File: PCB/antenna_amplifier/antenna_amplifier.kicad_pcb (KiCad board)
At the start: 4 copper layers, 200 x 100 mm, 131 parts, among them J101 PWR_IN 9V, J201 FILT_IN, J202 BIAS, J401 AES3 OUT, J402 S/PDIF OUT, SW301 RESET, SW302 PCM1804 MODE, SW401 CS8406 MODE, U101 ADM7150ARDZ-5.0, U102 ADM7150ARDZ-3.3, U201 LMP7721, U202 LMP7715, U203 LMP7715, U301 LMP7715, U302 PCM1804, U401 CS8406, Y401 24.576MHz

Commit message: Add mechanical design, PSU placement table and status notes (checkpoint)
mechanical/: CadQuery sources, STEP, DXF and renders for the amplifier
shield (7 mm flat-bar frame, milled tray, lid), PSU box, air-gap plate
capacitor assembly and the outdoor enclosure fit check (Fibox ARCA
403015). STATUS.md lists what is done and the next steps.

Co-Authored-By: Claude Opus 5.5 <noreply@anthropic.com>
Claude-Session: https://claude.ai/code/session_01RsM1DhHhY1tSr2aHjVygSC
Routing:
- added copper zone on In1.Cu, net GND

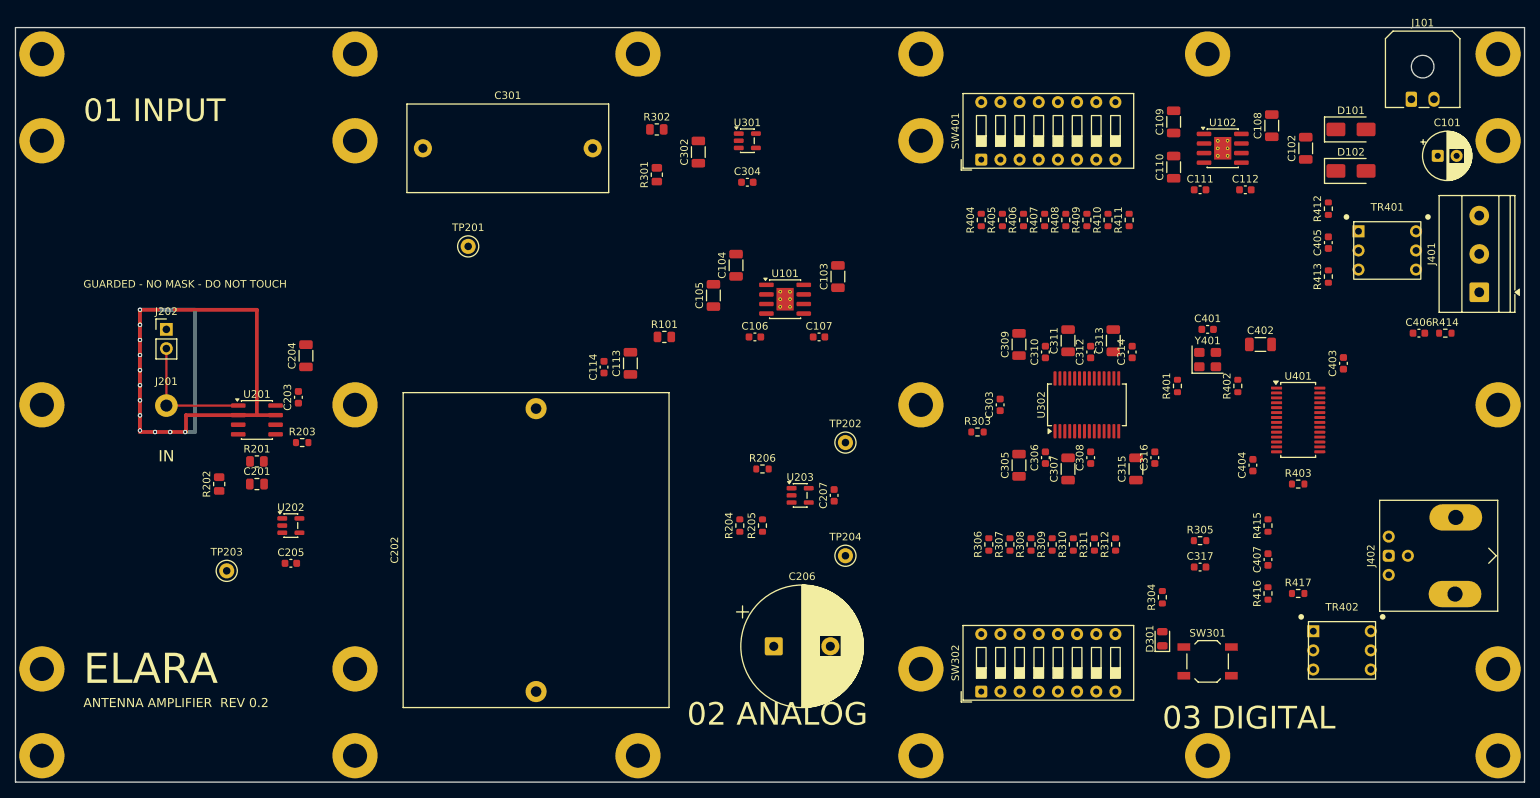
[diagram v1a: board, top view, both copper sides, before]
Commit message: Route the amplifier board: fully connected, DRC clean
GND fan-out to the In1 plane before routing, GND kept in the router copy,
ADM7150 exposed pads and LMP7721 V- get their own vias.

Co-Authored-By: Claude Opus 5.5 <noreply@anthropic.com>
Claude-Session: https://claude.ai/code/session_01RsM1DhHhY1tSr2aHjVygSC
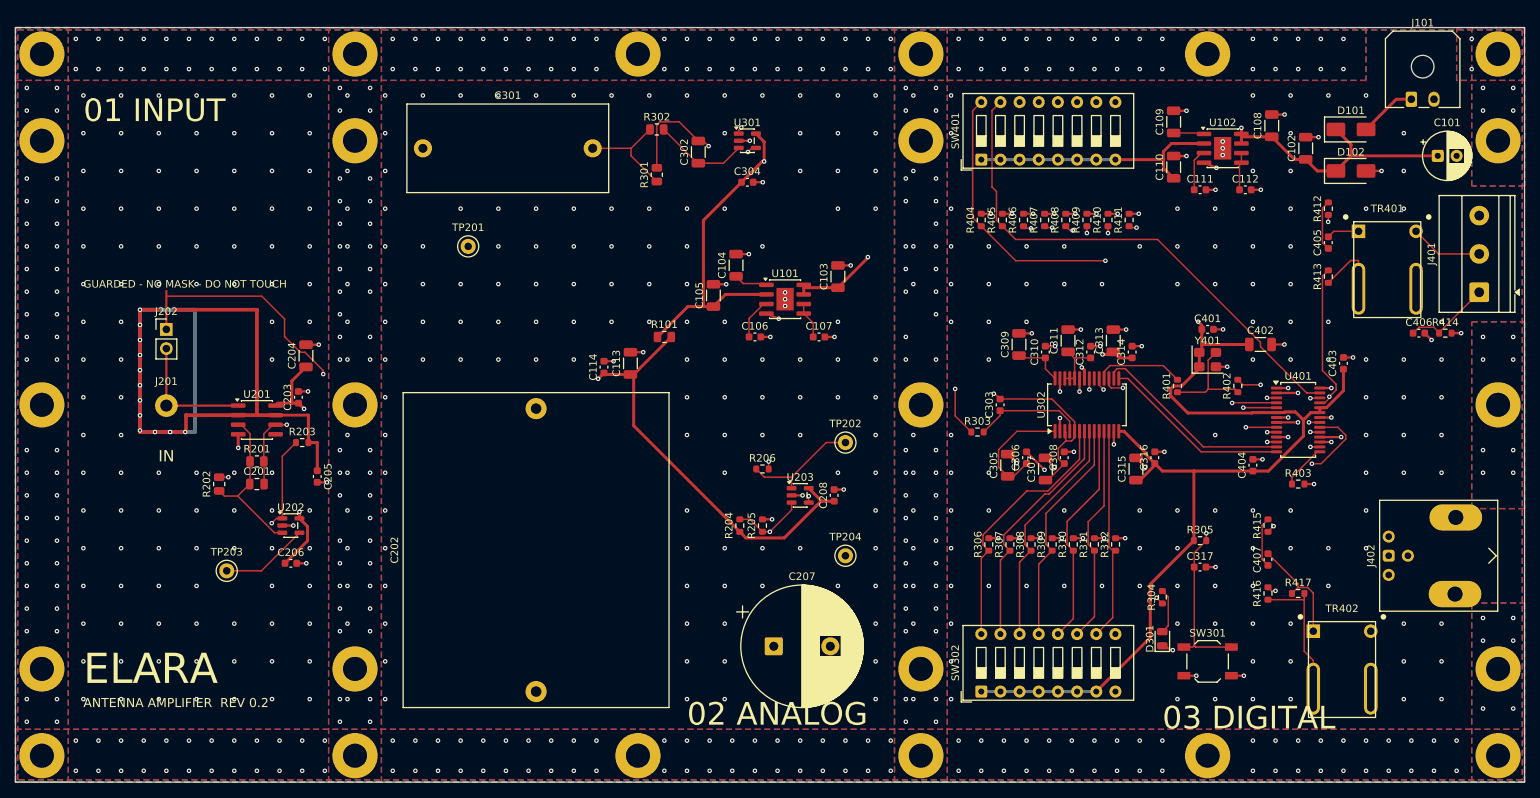
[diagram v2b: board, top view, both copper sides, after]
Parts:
- added C208: 100n, Capacitor_SMD:C_0603_1608Metric, F.Cu at (158.5, 112.0)
- C205: value 100n -> 220p
- C206: value 4700u -> 100n; footprint Capacitor_THT:CP_Radial_D16.0mm_P7.50mm -> Capacitor_SMD:C_0603_1608Metric
- C207: value 100n -> 4700u; footprint Capacitor_SMD:C_0603_1608Metric -> Capacitor_THT:CP_Radial_D16.0mm_P7.50mm
- H1, H10, H11, H12, H13, H14, H15, H16, H17, H18, H19, H2, H20, H21, H22, H23, H24, H3, H4, H5, H6, H7, H8, H9: footprint (none) -> elara:MountingHole_M3_Strip
- TR401: footprint elara:Transformer_Pulse_DIP-6_W7.62mm -> elara:Transformer_Pulse_4Pin_W7.62mm
- TR402: value S22082 -> S22083; footprint elara:Transformer_Pulse_DIP-6_W7.62mm -> elara:Transformer_Pulse_4Pin_W7.62mm
- U101, U102: footprint Package_SO:SOIC-8-1EP_3.9x4.9mm_P1.27mm_EP2.29x3mm_ThermalVias -> Package_SO:SOIC-8-1EP_3.9x4.9mm_P1.27mm_EP2.29x3mm
- moved C206 64.9 mm to (86.5, 121.0)
- moved C207 21.5 mm to (150.5, 132.0), turned to 0 degrees
- moved C205 12.0 mm to (90.0, 109.5), turned to -90 degrees
- moved C308 3.50 mm to (189.0, 107.0)
- moved C307 3.00 mm to (186.5, 108.5)
- moved C306 2.50 mm to (184.0, 107.0)
- moved C305 1.50 mm to (181.5, 108.0)
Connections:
- C205 pad 1: +5V_PRE -> GUARD
- C206 pad 1: BIAS_DIV -> +5V_PRE
- C207 pad 1: +5V_PRE -> BIAS_DIV
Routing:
- net +3V3: track 0.00 -> 192.1 mm, vias 0 -> 1
- net +5V_PRE: track 0.00 -> 128.9 mm, vias 0 -> 3
- net GND: track 0.00 -> 122.7 mm, vias 0 -> 786
- net +9V: track 0.00 -> 111.3 mm, vias 0 -> 2
- net +5VA: track 0.00 -> 106.5 mm, vias 0 -> 3
- net ANT_BIAS: track 0.00 -> 96.6 mm, vias 0 -> 2
- net VCOML: track 0.00 -> 89.9 mm, vias 0 -> 2
- net HWCK0: track 0.00 -> 84.7 mm, vias 0 -> 2
- net HWCK1: track 0.00 -> 69.0 mm
- net RESET_N: track 0.00 -> 61.9 mm, vias 0 -> 3
- net CEN: track 0.00 -> 61.4 mm, vias 0 -> 2
- net SFMT0: track 0.00 -> 60.7 mm, vias 0 -> 2
- net PREAMP_OUT: track 0.00 -> 59.8 mm, vias 0 -> 1
- net SFMT1: track 0.00 -> 58.1 mm, vias 0 -> 2
- net APMS: track 0.00 -> 57.9 mm, vias 0 -> 2
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- added copper zone on B.Cu, net GND
- added copper zone on F.Cu, net GND
- added copper zone on In2.Cu, net GND

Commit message: Amplifier silkscreen: labels placed clear of parts, references tidied
Board texts go to the nearest free spot; each reference moves to a spot clear
of pads, silk and mask openings, or is hidden where none fits (F.Fab keeps it).
Guard-ring gap ends on vias, ANT_BIAS stub trimmed: no dangling copper.

Co-Authored-By: Claude Opus 5.5 <noreply@anthropic.com>
Claude-Session: https://claude.ai/code/session_01RsM1DhHhY1tSr2aHjVygSC
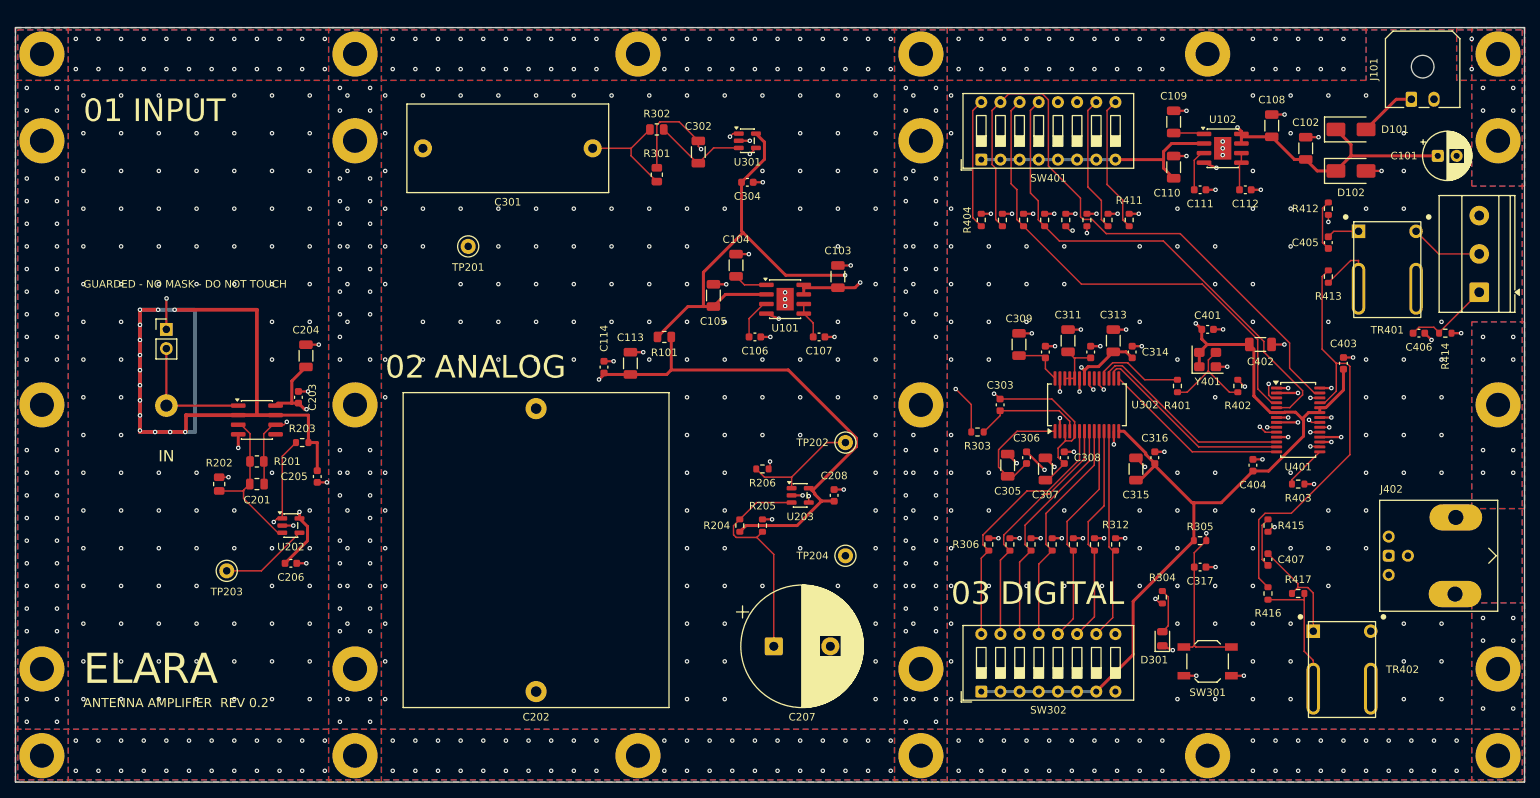
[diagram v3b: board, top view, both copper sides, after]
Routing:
- net AUDIO_N: track 57.1 -> 74.2 mm, vias 2 -> 1
- net HWCK0: track 84.7 -> 101.5 mm, vias 2 -> 1
- net EMPH_N: track 50.7 -> 67.5 mm, vias 2 -> 1
- net HWCK1: track 69.0 -> 85.2 mm
- net ANT_BIAS: track 96.6 -> 111.9 mm
- net +5V_PRE: track 128.9 -> 142.8 mm
- net +3V3: track 192.1 -> 181.2 mm
- net TXN: track 49.8 -> 58.7 mm, vias 2 -> 0
- net SFMT1: track 58.1 -> 66.4 mm, vias 2 -> 0
- net BIAS_DIV: track 25.1 -> 29.8 mm, vias 1 -> 0
- net SFMT0: track 60.7 -> 64.6 mm, vias 2 -> 0
- net +9V: track 111.3 -> 108.6 mm
- net LRCK: track 26.3 -> 27.6 mm, vias 2 -> 0
- net +5VA: track 106.5 -> 105.2 mm, vias 3 -> 2
- net RESET_N: track 61.9 -> 62.7 mm
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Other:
- board text added: "4 LAYER 1.6 MM CERN-OHL-W-2.0"
- board text added: "ANTENNA FROM BELOW"
- board text added: "ELF ATMOSPHERIC RADIO ANALYSER"
- board text removed: "ANTENNA AMPLIFIER REV 0.2 4 LAYER 1.6 MM"
- board text removed: "ANTENNA INPUT FROM BELOW"
- board text removed: "CERN-OHL-W-2.0"
- board text removed: "ELARA ELF ATMOSPHERIC RADIO ANALYSER"

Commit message: Leaded SOT23-5 oscillator (SiT2001B, Y402) fitted; SiT1602 kept as do-not-fit alternative
Hand-soldering friendly: Y402 sits under Y401 between the two clock series
resistors, both wired to OSC_OUT (outputs typed tri-state; fit only one).
Board re-routed: 0 DRC errors, 0 unconnected. Fitted parts get silkscreen
label priority over do-not-fit ones. Fab outputs now include populated STEP
models of both boards; BOM, assembly guide and open checks updated.

Co-Authored-By: Claude Opus 5.5 <noreply@anthropic.com>
Claude-Session: https://claude.ai/code/session_01RsM1DhHhY1tSr2aHjVygSC
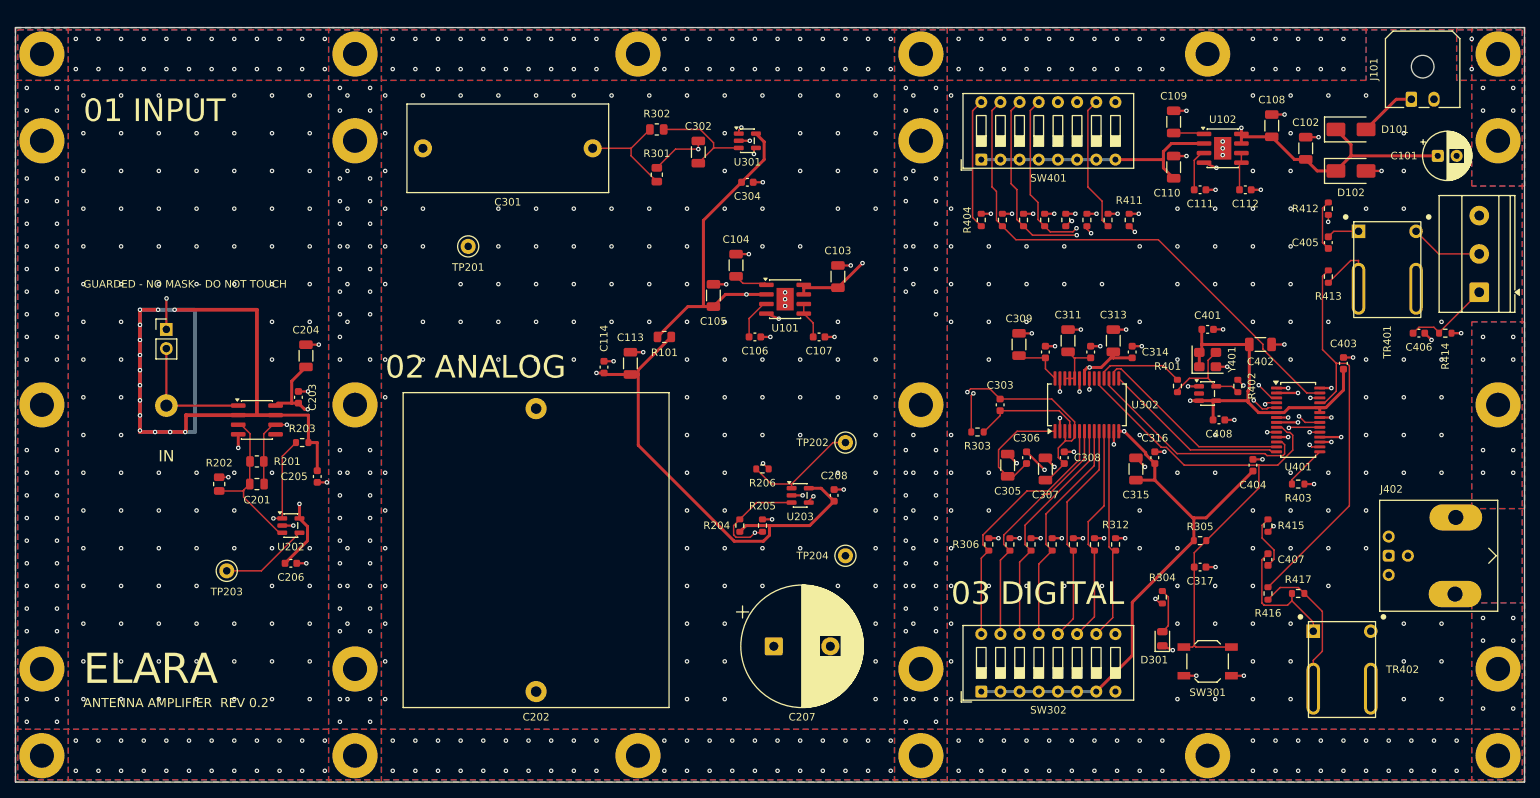
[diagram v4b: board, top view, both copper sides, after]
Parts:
- added C408: 100n, Capacitor_SMD:C_0603_1608Metric, F.Cu at (209.5, 102.0)
- added Y402: 24.576MHz, Package_TO_SOT_SMD:SOT-23-5, F.Cu at (208.0, 98.5)
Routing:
- net +3V3: track 181.2 -> 203.2 mm, vias 1 -> 2
- net AUDIO_N: track 74.2 -> 56.8 mm, vias 1 -> 2
- net HWCK1: track 85.2 -> 69.1 mm
- net HWCK0: track 101.5 -> 89.1 mm
- net RESET_N: track 62.7 -> 70.2 mm, vias 3 -> 0
- net SFMT1: track 66.4 -> 59.0 mm, vias 0 -> 2
- net VCOML: track 90.1 -> 84.8 mm
- net +5V_PRE: track 142.8 -> 138.4 mm
- net SFMT0: track 64.6 -> 61.1 mm, vias 0 -> 2
- net TXN: track 58.7 -> 55.6 mm
- net LRCK: track 27.6 -> 30.6 mm
- net COAX_P1: track 14.6 -> 17.4 mm
- net GND: track 122.7 -> 125.4 mm, vias 779 -> 784
- net +9V: track 108.6 -> 111.3 mm
- net COAX_P2: track 17.9 -> 19.9 mm
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
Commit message: Pedantic DRC/ERC pass: schematic parity clean, BNC notch, island without silk
- Board nets carry the schematic's names (sheet-path prefix on local nets, KiCad's
  unconnected-(...) nets on open pins): DRC schematic parity 0 on both boards.
- BNC: its mounting lugs reached 1.4 mm under the right-hand wall, whose round
  barrel hole left the bar resting on them (tilted wall, BNC shell = S/PDIF return
  shorted to the shield). The frame now has a 16 x 14 mm notch there, and the
  strip copper stops clear of the lugs. Micro-Fit notch widened to 14 mm.
- Guard island: mask opening follows the island outline; LMP7721 and the bias link
  use project footprint variants without silk on the island (no ink on the
  femtoamp surface). tools/fp_variants.py derives them from the stock footprints.
- S22083 footprint: silk outline no longer crosses its own slotted pads.
- CS8406 as a project symbol with pin 1 typed as the hardware-mode COPY/C input:
  ERC 0 on both schematics. PSU mounting holes out of the BOM; plate and PSU
  projects register the elara footprint library.
- Remaining amplifier DRC items: 79 solder-mask-bridge warnings, all on the
  deliberately unmasked guard island. PSU and plate boards: 0 of anything.

Co-Authored-By: Claude Opus 5.5 <noreply@anthropic.com>
Claude-Session: https://claude.ai/code/session_01RsM1DhHhY1tSr2aHjVygSC
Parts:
- J202: footprint Connector_PinHeader_2.54mm:PinHeader_1x02_P2.54mm_Vertical -> elara:PinHeader_1x02_P2.54mm_Vertical_NoSilk
- U201: footprint Package_SO:SOIC-8_3.9x4.9mm_P1.27mm -> elara:SOIC-8_3.9x4.9mm_P1.27mm_GuardIsland
- moved C101 0.50 mm to (238.0, 67.0)
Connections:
- net ADC_A renamed /ADC (PCM1804)/ADC_A
- net AES_A renamed /Clock and S/PDIF + AES3 output/AES_A
- net AES_COLD renamed /Clock and S/PDIF + AES3 output/AES_COLD
- net AES_HOT renamed /Clock and S/PDIF + AES3 output/AES_HOT
- net AES_P1 renamed /Clock and S/PDIF + AES3 output/AES_P1
- net AES_P2 renamed /Clock and S/PDIF + AES3 output/AES_P2
- net AES_SHIELD renamed /Clock and S/PDIF + AES3 output/AES_SHIELD
- net ANT_BIAS renamed /Electrometer front end/ANT_BIAS
- net APMS renamed /Clock and S/PDIF + AES3 output/APMS
- net AUDIO_N renamed /Clock and S/PDIF + AES3 output/AUDIO_N
- net BIAS_BUF renamed /Electrometer front end/BIAS_BUF
- net BIAS_DIV renamed /Electrometer front end/BIAS_DIV
- net BYPAS renamed /ADC (PCM1804)/BYPAS
- net BYP_A renamed /Power input and regulators/BYP_A
- net BYP_D renamed /Power input and regulators/BYP_D
- net CEN renamed /Clock and S/PDIF + AES3 output/CEN
- net CG renamed /Electrometer front end/CG
- net COAX_A renamed /Clock and S/PDIF + AES3 output/COAX_A
- net COAX_P1 renamed /Clock and S/PDIF + AES3 output/COAX_P1
- net COAX_P2 renamed /Clock and S/PDIF + AES3 output/COAX_P2
- net DRV_OUT renamed /ADC (PCM1804)/DRV_OUT
- net EMPH_N renamed /Clock and S/PDIF + AES3 output/EMPH_N
- net FMT0 renamed /ADC (PCM1804)/FMT0
- net FMT1 renamed /ADC (PCM1804)/FMT1
- net GUARD renamed /Electrometer front end/GUARD
- net GUARD_DRV renamed /Electrometer front end/GUARD_DRV
- net HWCK0 renamed /Clock and S/PDIF + AES3 output/HWCK0
- net HWCK1 renamed /Clock and S/PDIF + AES3 output/HWCK1
- net IN_N renamed /Electrometer front end/IN_N
- net IN_P renamed /Electrometer front end/IN_P
- net LED_OVF renamed /ADC (PCM1804)/LED_OVF
- net MCLK_TX renamed /Clock and S/PDIF + AES3 output/MCLK_TX
- net OSC_OUT renamed /Clock and S/PDIF + AES3 output/OSC_OUT
- net OSR0 renamed /ADC (PCM1804)/OSR0
- net OSR1 renamed /ADC (PCM1804)/OSR1
- net OSR2 renamed /ADC (PCM1804)/OSR2
- net OVFL renamed /ADC (PCM1804)/OVFL
- net REF_A renamed /Power input and regulators/REF_A
- net REF_D renamed /Power input and regulators/REF_D
- net SFMT0 renamed /Clock and S/PDIF + AES3 output/SFMT0
- net SFMT1 renamed /Clock and S/PDIF + AES3 output/SFMT1
- net SM renamed /ADC (PCM1804)/SM
- net SPDIF_OUT renamed /Clock and S/PDIF + AES3 output/SPDIF_OUT
- net SPDIF_RET renamed /Clock and S/PDIF + AES3 output/SPDIF_RET
- net TCBL renamed /Clock and S/PDIF + AES3 output/TCBL
- net TXN renamed /Clock and S/PDIF + AES3 output/TXN
- net TXP renamed /Clock and S/PDIF + AES3 output/TXP
- net VCOML renamed /ADC (PCM1804)/VCOML
- net VCOMR renamed /ADC (PCM1804)/VCOMR
- net VINL renamed /ADC (PCM1804)/VINL
- net VINL_F renamed /ADC (PCM1804)/VINL_F
- net VIN_RAW renamed /Power input and regulators/VIN_RAW
- net VREFL renamed /ADC (PCM1804)/VREFL
- net VREFR renamed /ADC (PCM1804)/VREFR
- net VREG_A renamed /Power input and regulators/VREG_A
- net VREG_D renamed /Power input and regulators/VREG_D
- SW302 pad 8: (no net) -> unconnected-(SW302-Pad8)
- SW302 pad 9: (no net) -> unconnected-(SW302-Pad9)
- U201 pad 5: (no net) -> unconnected-(U201-Pad5)
- U302 pad 20: (no net) -> unconnected-(U302-OVFR-Pad20)
- Y402 pad 2: (no net) -> unconnected-(Y402-NC-Pad2)
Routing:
- net /Clock and S/PDIF + AES3 output/CEN: track 62.3 -> 78.6 mm, vias 2 -> 1
- net +9V: track 111.3 -> 113.8 mm
- net +3V3: track 203.2 -> 205.4 mm
- net /ADC (PCM1804)/VCOML: track 84.8 -> 86.8 mm
- net +5VA: track 105.3 -> 106.6 mm, vias 2 -> 3
- net /ADC (PCM1804)/DRV_OUT: track 55.1 -> 56.0 mm
- net /Clock and S/PDIF + AES3 output/SFMT1: track 59.0 -> 58.4 mm
- net GND: vias 784 -> 788
